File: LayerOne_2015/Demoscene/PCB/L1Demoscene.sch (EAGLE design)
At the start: 50 parts, among them IC1 MEGA8-AI, IC2 REG1117, J1 AVR_SPI_PRG_6PTH

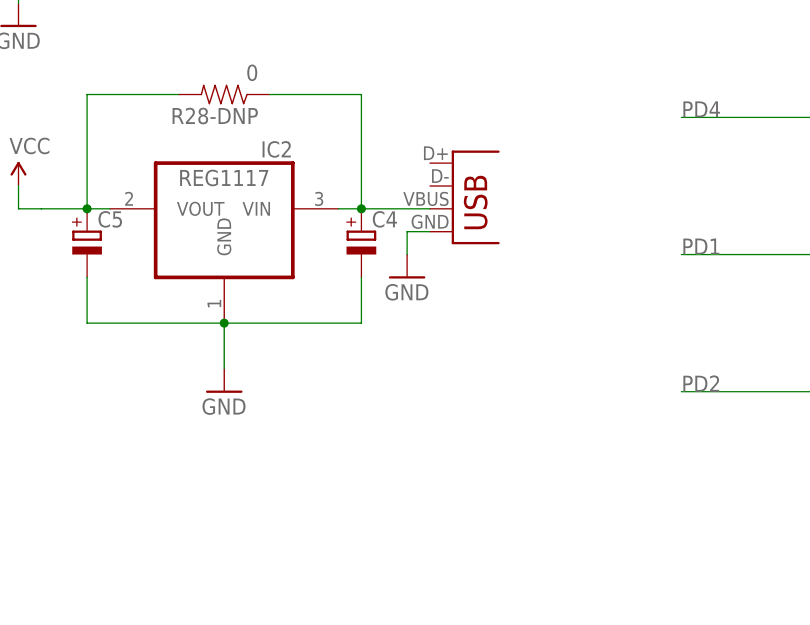
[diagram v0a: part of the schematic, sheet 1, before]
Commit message: 
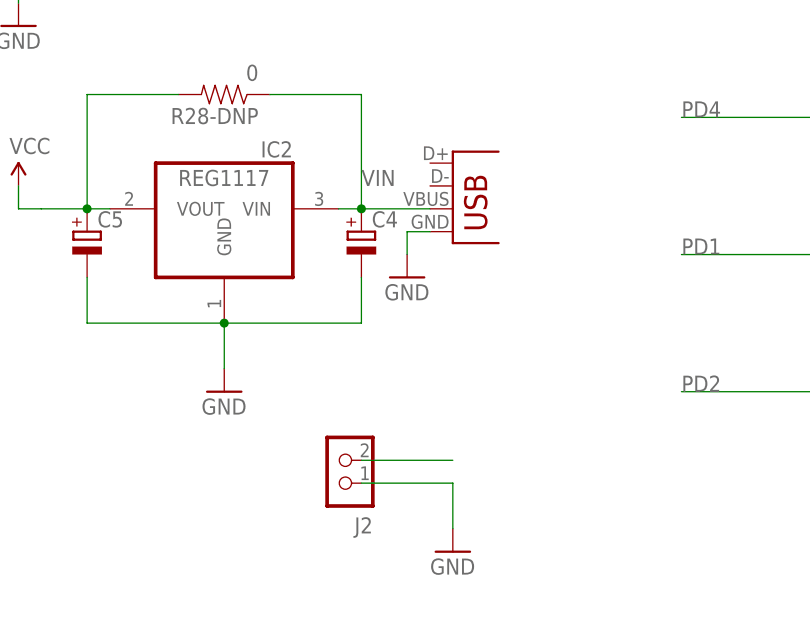
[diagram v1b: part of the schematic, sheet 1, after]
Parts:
- added J2: CON_HEADER_1X02-PTH, dp_devices:CON_HEADER_1X02-PTH
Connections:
- removed net N$13: C4.+, IC2.VIN, JP3.VBUS, R28-DNP.1
- new net VIN: C4.+, IC2.VIN, J2.2, JP3.VBUS, R28-DNP.1
- net GND: now also J2.1
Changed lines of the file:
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@@
 <part name="C7" library="SparkFun-Capacitors" deviceset="CAP" device="0603-CAP" value="100nf"/>
 <part name="GND16" library="SparkFun-Aesthetics" deviceset="GND" device=""/>
+<part name="J2" library="dp_devices" deviceset="CON_HEADER_1X02" device="-PTH"/>
+<part name="GND17" library="SparkFun-Aesthetics" deviceset="GND" device=""/>
 </parts>
 <sheets>
@@
 <instance part="C7" gate="G$1" x="55.88" y="66.04" rot="R180"/>
 <instance part="GND16" gate="1" x="55.88" y="55.88"/>
+<instance part="J2" gate="J" x="180.34" y="-48.26" rot="R180"/>
+<instance part="GND17" gate="1" x="190.5" y="-55.88"/>
 </instances>
 <busses>
@@
 <pinref part="C7" gate="G$1" pin="1"/>
 <wire x1="55.88" y1="58.42" x2="55.88" y2="60.96" width="0.1524" layer="91"/>
+</segment>
+<segment>
+<pinref part="J2" gate="J" pin="1"/>
+<wire x1="180.34" y1="-48.26" x2="190.5" y2="-48.26" width="0.1524" layer="91"/>
+<wire x1="190.5" y1="-48.26" x2="190.5" y2="-53.34" width="0.1524" layer="91"/>
+<pinref part="GND17" gate="1" pin="GND"/>
 </segment>
 </net>
@@
 </segment>
 </net>
-<net name="N$13" class="0">
+<net name="VIN" class="0">
 <segment>
 <pinref part="JP3" gate="G$1" pin="VBUS"/>
@@
 <pinref part="C4" gate="C" pin="+"/>
 <junction x="180.34" y="-17.78"/>
-</segment>
-</net>
+<label x="180.34" y="-15.24" size="1.778" layer="95"/>
+</segment>
+<segment>
+<pinref part="J2" gate="J" pin="2"/>
+<wire x1="180.34" y1="-45.72" x2="190.5" y2="-45.72" width="0.1524" layer="91"/>
+</segment>
+</net>

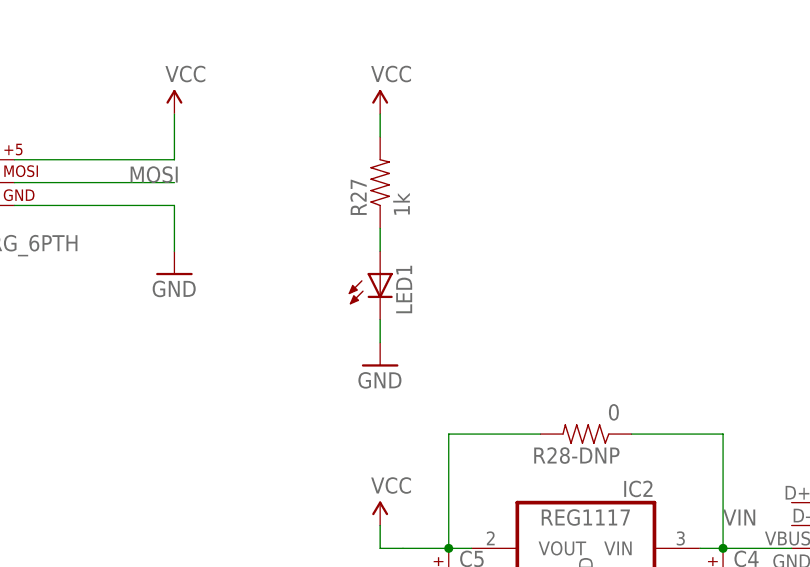
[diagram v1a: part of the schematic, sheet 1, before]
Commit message: 
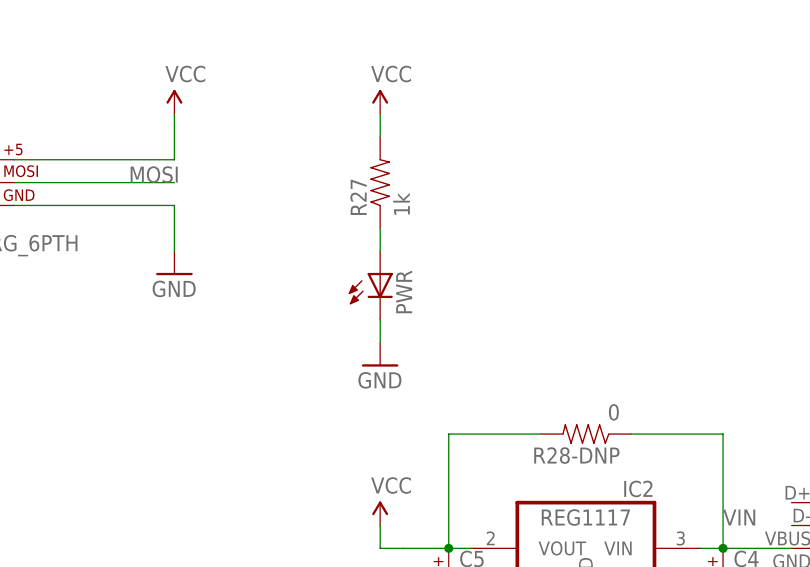
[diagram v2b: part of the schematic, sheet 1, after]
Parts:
- renumbered LED1 to PWR
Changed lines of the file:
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@@
 <part name="GND12" library="SparkFun-Aesthetics" deviceset="GND" device=""/>
 <part name="R27" library="SparkFun-Resistors" deviceset="RESISTOR" device="0603-RES" value="1k"/>
-<part name="LED1" library="dp_devices" deviceset="LED" device="-0603"/>
+<part name="PWR" library="dp_devices" deviceset="LED" device="-0603"/>
 <part name="SUPPLY6" library="SparkFun-Aesthetics" deviceset="VCC" device=""/>
 <part name="GND13" library="SparkFun-Aesthetics" deviceset="GND" device=""/>
@@
 <instance part="GND12" gate="1" x="185.42" y="-25.4"/>
 <instance part="R27" gate="G$1" x="142.24" y="22.86" rot="R90"/>
-<instance part="LED1" gate="LED" x="142.24" y="12.7"/>
+<instance part="PWR" gate="LED" x="142.24" y="12.7"/>
 <instance part="SUPPLY6" gate="1" x="142.24" y="30.48"/>
 <instance part="GND13" gate="1" x="142.24" y="2.54"/>
@@
 </segment>
 <segment>
-<pinref part="LED1" gate="LED" pin="C"/>
+<pinref part="PWR" gate="LED" pin="C"/>
 <pinref part="GND13" gate="1" pin="GND"/>
 <wire x1="142.24" y1="7.62" x2="142.24" y2="5.08" width="0.1524" layer="91"/>
@@
 <segment>
 <pinref part="R27" gate="G$1" pin="1"/>
-<pinref part="LED1" gate="LED" pin="A"/>
+<pinref part="PWR" gate="LED" pin="A"/>
 <wire x1="142.24" y1="17.78" x2="142.24" y2="15.24" width="0.1524" layer="91"/>
 </segment>

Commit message: added LED and Button
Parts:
- added LED1: (no value), dp_devices:LED-0603
- added R28: 1k, SparkFun-Resistors:RESISTOR0603-RES
- added S2: Switch, tvbgone-2layer:SPARKFUN-ELECTROMECHANICAL_SWITCH-MOMENTARY-2-SMD-1101NE
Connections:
- new net N$13: LED1.A, R28.1
- new net PB0: IC1.PB0(ICP), R28.2
- new net PD0: IC1.PD0(RXD), S2.2
- net GND: now also LED1.C, S2.1
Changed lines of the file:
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@@
 <part name="J2" library="dp_devices" deviceset="CON_HEADER_1X02" device="-PTH"/>
 <part name="GND17" library="SparkFun-Aesthetics" deviceset="GND" device=""/>
+<part name="R28" library="SparkFun-Resistors" deviceset="RESISTOR" device="0603-RES" value="1k"/>
+<part name="LED1" library="dp_devices" deviceset="LED" device="-0603"/>
+<part name="GND18" library="SparkFun-Aesthetics" deviceset="GND" device=""/>
+<part name="S2" library="tvbgone-2layer" deviceset="SPARKFUN-ELECTROMECHANICAL_SWITCH-MOMENTARY-2" device="-SMD-1101NE" value="Switch"/>
+<part name="GND19" library="SparkFun-Aesthetics" deviceset="GND" device=""/>
 </parts>
 <sheets>
@@
 <instance part="R27" gate="G$1" x="142.24" y="22.86" rot="R90"/>
 <instance part="PWR" gate="LED" x="142.24" y="12.7"/>
-<instance part="SUPPLY6" gate="1" x="142.24" y="30.48"/>
+<instance part="SUPPLY6" gate="1" x="142.24" y="35.56"/>
 <instance part="GND13" gate="1" x="142.24" y="2.54"/>
 <instance part="IC2" gate="G$1" x="165.1" y="-17.78" rot="MR0"/>
@@
 <instance part="J2" gate="J" x="180.34" y="-48.26" rot="R180"/>
 <instance part="GND17" gate="1" x="190.5" y="-55.88"/>
+<instance part="R28" gate="G$1" x="154.94" y="25.4" rot="R90"/>
+<instance part="LED1" gate="LED" x="154.94" y="15.24"/>
+<instance part="GND18" gate="1" x="154.94" y="5.08"/>
+<instance part="S2" gate="G$1" x="167.64" y="17.78" rot="R90"/>
+<instance part="GND19" gate="1" x="167.64" y="5.08"/>
 </instances>
 <busses>
@@
 <wire x1="190.5" y1="-48.26" x2="190.5" y2="-53.34" width="0.1524" layer="91"/>
 <pinref part="GND17" gate="1" pin="GND"/>
+</segment>
+<segment>
+<pinref part="LED1" gate="LED" pin="C"/>
+<pinref part="GND18" gate="1" pin="GND"/>
+<wire x1="154.94" y1="10.16" x2="154.94" y2="7.62" width="0.1524" layer="91"/>
+</segment>
+<segment>
+<pinref part="S2" gate="G$1" pin="1"/>
+<wire x1="167.64" y1="12.7" x2="167.64" y2="7.62" width="0.1524" layer="91"/>
+<pinref part="GND19" gate="1" pin="GND"/>
 </segment>
 </net>
@@
 <pinref part="SUPPLY6" gate="1" pin="VCC"/>
 <pinref part="R27" gate="G$1" pin="2"/>
-<wire x1="142.24" y1="30.48" x2="142.24" y2="27.94" width="0.1524" layer="91"/>
+<wire x1="142.24" y1="35.56" x2="142.24" y2="27.94" width="0.1524" layer="91"/>
 </segment>
 <segment>
@@
 </segment>
 </net>
+<net name="N$13" class="0">
+<segment>
+<pinref part="R28" gate="G$1" pin="1"/>
+<pinref part="LED1" gate="LED" pin="A"/>
+<wire x1="154.94" y1="20.32" x2="154.94" y2="17.78" width="0.1524" layer="91"/>
+</segment>
+</net>
+<net name="PB0" class="0">
+<segment>
+<pinref part="IC1" gate="G$1" pin="PB0(ICP)"/>
+<wire x1="116.84" y1="63.5" x2="132.08" y2="63.5" width="0.1524" layer="91"/>
+<label x="127" y="63.5" size="1.778" layer="95"/>
+</segment>
+<segment>
+<pinref part="R28" gate="G$1" pin="2"/>
+<wire x1="154.94" y1="30.48" x2="154.94" y2="38.1" width="0.1524" layer="91"/>
+<label x="154.94" y="38.1" size="1.778" layer="95"/>
+</segment>
+</net>
+<net name="PD0" class="0">
+<segment>
+<pinref part="IC1" gate="G$1" pin="PD0(RXD)"/>
+<wire x1="116.84" y1="86.36" x2="132.08" y2="86.36" width="0.1524" layer="91"/>
+<label x="127" y="86.36" size="1.778" layer="95"/>
+</segment>
+<segment>
+<pinref part="S2" gate="G$1" pin="2"/>
+<wire x1="167.64" y1="22.86" x2="167.64" y2="38.1" width="0.1524" layer="91"/>
+<label x="167.64" y="38.1" size="1.778" layer="95"/>
+</segment>
+</net>

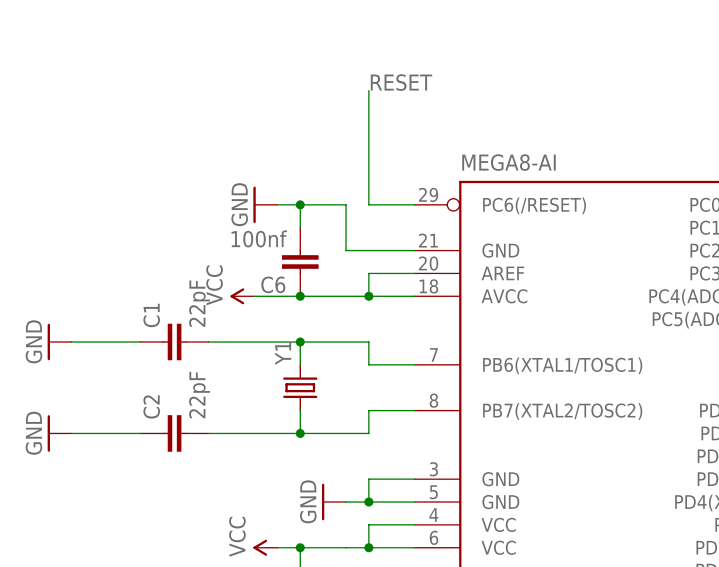
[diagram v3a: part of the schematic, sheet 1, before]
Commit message: added NC jumper to AVcc pin
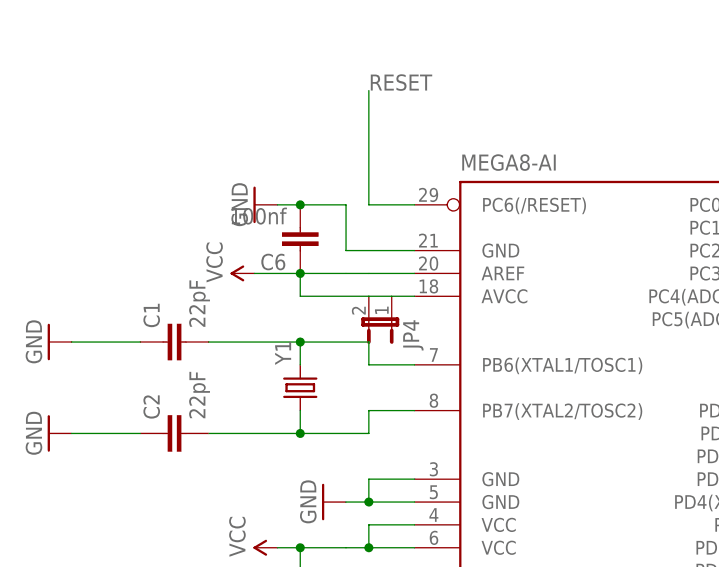
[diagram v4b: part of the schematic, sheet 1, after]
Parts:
- added JP4: (no value), SparkFun-Passives:JUMPER-2SMD-NC
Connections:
- net VCC: now also JP4.1, JP4.2
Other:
- moved on the sheet: C6
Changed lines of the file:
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@@
 <part name="S2" library="tvbgone-2layer" deviceset="SPARKFUN-ELECTROMECHANICAL_SWITCH-MOMENTARY-2" device="-SMD-1101NE" value="Switch"/>
 <part name="GND19" library="SparkFun-Aesthetics" deviceset="GND" device=""/>
+<part name="JP4" library="SparkFun-Passives" deviceset="JUMPER-2" device="SMD-NC"/>
 </parts>
 <sheets>
@@
 <instance part="GND3" gate="1" x="58.42" y="76.2" rot="R270"/>
 <instance part="SUPPLY1" gate="1" x="53.34" y="71.12" rot="R90"/>
-<instance part="SUPPLY2" gate="1" x="50.8" y="99.06" rot="R90"/>
+<instance part="SUPPLY2" gate="1" x="50.8" y="101.6" rot="R90"/>
 <instance part="GND4" gate="1" x="50.8" y="109.22" rot="R270"/>
 <instance part="R2" gate="G$1" x="203.2" y="127"/>
@@
 <instance part="S1" gate="G$1" x="60.96" y="10.16" rot="R90"/>
 <instance part="GND15" gate="1" x="60.96" y="-2.54"/>
-<instance part="C6" gate="G$1" x="55.88" y="104.14" rot="R180"/>
+<instance part="C6" gate="G$1" x="55.88" y="106.68" rot="R180"/>
 <instance part="C7" gate="G$1" x="55.88" y="66.04" rot="R180"/>
 <instance part="GND16" gate="1" x="55.88" y="55.88"/>
@@
 <instance part="S2" gate="G$1" x="167.64" y="17.78" rot="R90"/>
 <instance part="GND19" gate="1" x="167.64" y="5.08"/>
+<instance part="JP4" gate="A" x="66.04" y="96.52" rot="R180"/>
 </instances>
 <busses>
@@
 <pinref part="IC1" gate="G$1" pin="GND"/>
 <pinref part="C6" gate="G$1" pin="2"/>
-<wire x1="55.88" y1="106.68" x2="55.88" y2="109.22" width="0.1524" layer="91"/>
 <junction x="55.88" y="109.22"/>
 </segment>
@@
 </segment>
 <segment>
+<pinref part="SUPPLY2" gate="1" pin="VCC"/>
+<pinref part="IC1" gate="G$1" pin="AREF"/>
+<wire x1="60.96" y1="101.6" x2="55.88" y2="101.6" width="0.1524" layer="91"/>
+<wire x1="55.88" y1="101.6" x2="50.8" y2="101.6" width="0.1524" layer="91"/>
+<wire x1="68.58" y1="101.6" x2="63.5" y2="101.6" width="0.1524" layer="91"/>
+<wire x1="63.5" y1="101.6" x2="60.96" y2="101.6" width="0.1524" layer="91"/>
+<pinref part="C6" gate="G$1" pin="1"/>
+<junction x="55.88" y="101.6"/>
+<pinref part="JP4" gate="A" pin="2"/>
+<wire x1="63.5" y1="99.06" x2="55.88" y2="99.06" width="0.1524" layer="91"/>
+<wire x1="55.88" y1="99.06" x2="55.88" y2="101.6" width="0.1524" layer="91"/>
 <pinref part="IC1" gate="G$1" pin="AVCC"/>
-<pinref part="SUPPLY2" gate="1" pin="VCC"/>
-<wire x1="68.58" y1="99.06" x2="63.5" y2="99.06" width="0.1524" layer="91"/>
-<pinref part="IC1" gate="G$1" pin="AREF"/>
-<wire x1="63.5" y1="99.06" x2="55.88" y2="99.06" width="0.1524" layer="91"/>
-<wire x1="55.88" y1="99.06" x2="50.8" y2="99.06" width="0.1524" layer="91"/>
-<wire x1="68.58" y1="101.6" x2="63.5" y2="101.6" width="0.1524" layer="91"/>
-<wire x1="63.5" y1="101.6" x2="63.5" y2="99.06" width="0.1524" layer="91"/>
-<junction x="63.5" y="99.06"/>
-<pinref part="C6" gate="G$1" pin="1"/>
-<junction x="55.88" y="99.06"/>
-</segment>
-<segment>
+<wire x1="68.58" y1="99.06" x2="66.04" y2="99.06" width="0.1524" layer="91"/>
+<pinref part="JP4" gate="A" pin="1"/>
+<wire x1="63.5" y1="99.06" x2="66.04" y2="99.06" width="0.1524" layer="91"/>
+</segment>
+<segment>
